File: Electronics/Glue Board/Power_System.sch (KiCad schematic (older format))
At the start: 10 parts, among them J1 Conn_01x02_Male, J2 Barrel_Jack, U6 TPS2121RUXR

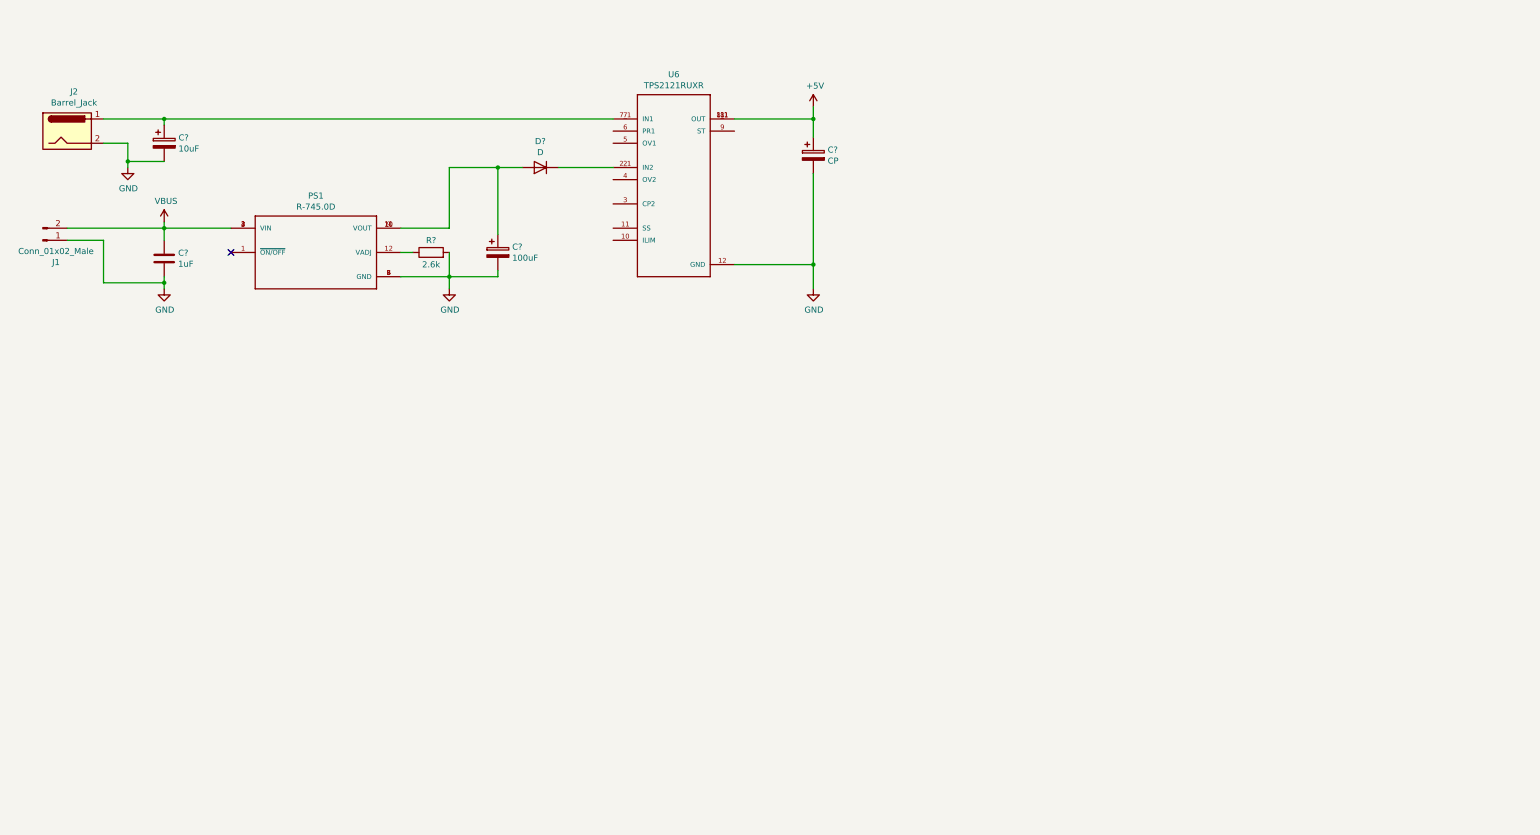
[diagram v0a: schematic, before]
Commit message: Finished the schematic for the most parts
Finished the schematic for the most parts
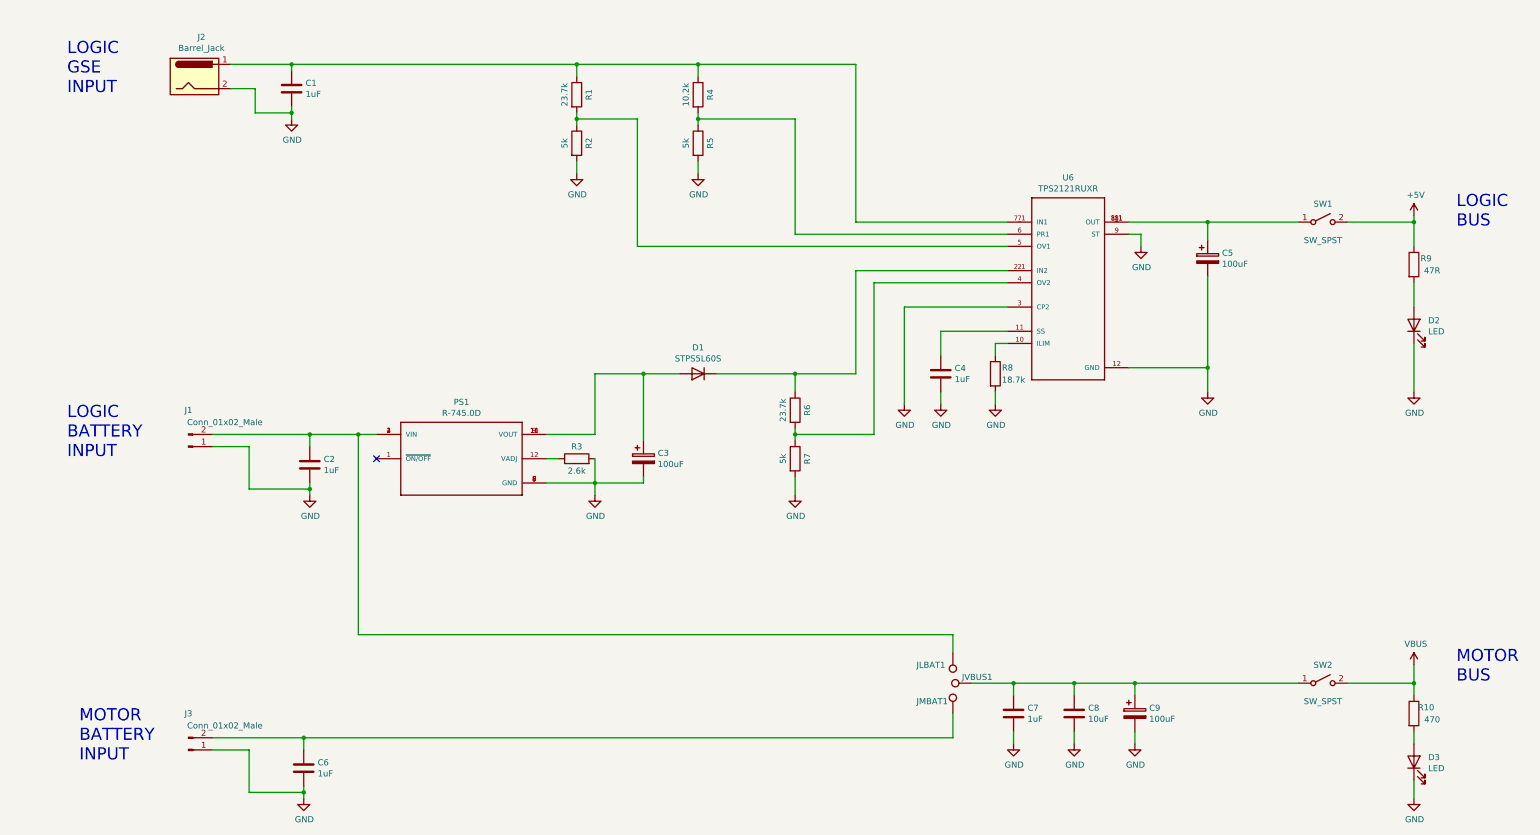
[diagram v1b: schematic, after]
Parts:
- removed C?: 10uF, symbol Device:CP
- added C1, C4, C6, C7: 1uF, Capacitor_SMD:C_0805_2012Metric, symbol Device:C
- added C8: 10uF, Capacitor_SMD:C_0805_2012Metric, symbol Device:C
- added C9: 100uF, Capacitor_SMD:C_1210_3225Metric, symbol Device:CP
- added D2, D3: LED, Connector_PinHeader_2.54mm:PinHeader_1x02_P2.54mm_Vertical, symbol Device:LED
- added J3: Conn_01x02_Male, Connector_AMASS:AMASS_XT30PW-M_1x02_P2.50mm_Horizontal, symbol Connector:Conn_01x02_Male
- added JLBAT1, JMBAT1, JVBUS1: TestPoint, TestPoint:TestPoint_Pad_D4.0mm, symbol Connector:TestPoint
- added R1, R6: 23.7k, Resistor_SMD:R_0603_1608Metric, symbol Device:R
- added R10: 470, Resistor_SMD:R_0603_1608Metric, symbol Device:R
- added R2, R5, R7: 5k, Resistor_SMD:R_0603_1608Metric, symbol Device:R
- added R4: 10.2k, Resistor_SMD:R_0603_1608Metric, symbol Device:R
- added R8: 18.7k, Resistor_SMD:R_0603_1608Metric, symbol Device:R
- added R9: 47R, Resistor_SMD:R_0603_1608Metric, symbol Device:R
- added SW1, SW2: SW_SPST, TerminalBlock:TerminalBlock_bornier-2_P5.08mm, symbol Switch:SW_SPST
- C2: renamed from C?; footprint (none) -> Capacitor_SMD:C_0805_2012Metric; MPN (none) -> C0805C105K4RACTU
- C3: renamed from C?; footprint (none) -> Capacitor_SMD:C_1210_3225Metric; MPN (none) -> C1210C107M4PAC7800
- C5: renamed from C?; value CP -> 100uF; footprint (none) -> Capacitor_SMD:C_1210_3225Metric; MPN (none) -> C1210C107M4PAC7800
- D1: renamed from D?; value D -> STPS5L60S; footprint (none) -> agg:DO-214AB-SMC; MPN (none) -> STPS5L60S
- PS1: Field4 9.10mm -> (none); Field5 RECOM -> (none); Field6 5 -> (none); MPN (none) -> R-745.0D
- R3: renamed from R?; footprint (none) -> Resistor_SMD:R_0603_1608Metric; MPN (none) -> RC0603FR-072K61L
- U6: Field4 Manufacturer Recommendations -> (none); MPN (none) -> TPS2121RUXR
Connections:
- net +5V: now also R9.1, SW1.2 (B); no longer C5.1, U6.1 (OUT), U6.1_1 (OUT), U6.8 (OUT), U6.8_1 (OUT)
- net GND: now also U6.3 (CP2), U6.9 (ST), C1.2, C4.2, C6.2, C7.2, C8.2, C9.2, D2.1 (K), D3.1 (K), J3.1 (Pin_1), R2.2, R5.2, R7.2, R8.2
- net VBUS: now also R10.1, SW2.2 (B); no longer C2.1, J1.2 (Pin_2), PS1.2 (VIN), PS1.3 (VIN), PS1.4 (VIN)
- net at U6.10 (ILIM): now also R8.1
- net at U6.11 (SS): now also C4.1
- net at D1.1 (K), U6.2 (IN2), U6.2_1 (IN2): now also R6.1
- net at U6.4 (OV2): now also R6.2, R7.1
- net at U6.5 (OV1): now also R1.2, R2.1
- net at U6.6 (PR1): now also R4.2, R5.1
- net at J2.1, U6.7 (IN1), U6.7_1 (IN1): now also C1.1, R1.1, R4.1
- new net: C2.1, J1.2 (Pin_2), JLBAT1.1, PS1.2 (VIN), PS1.3 (VIN), PS1.4 (VIN)
- new net: C5.1, SW1.1 (A), U6.1 (OUT), U6.1_1 (OUT), U6.8 (OUT), U6.8_1 (OUT)
- new net: C7.1, C8.1, C9.1, JVBUS1.1, SW2.1 (A)
- new net: C6.1, J3.2 (Pin_2), JMBAT1.1
- new net: D2.2 (A), R9.2
- new net: D3.2 (A), R10.2
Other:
- note added: "LOGIC\nBATTERY\nINPUT"
- note added: "LOGIC\nBUS"
- note added: "LOGIC\nGSE\nINPUT"
- note added: "MOTOR\nBATTERY\nINPUT"
- note added: "MOTOR\nBUS"
- moved on the sheet: C2, C3, C5, D1, J1, J2, PS1, R3, U6

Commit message: Complete Schematic and BOM
Complete Schematic and BOM. Next up, layout!
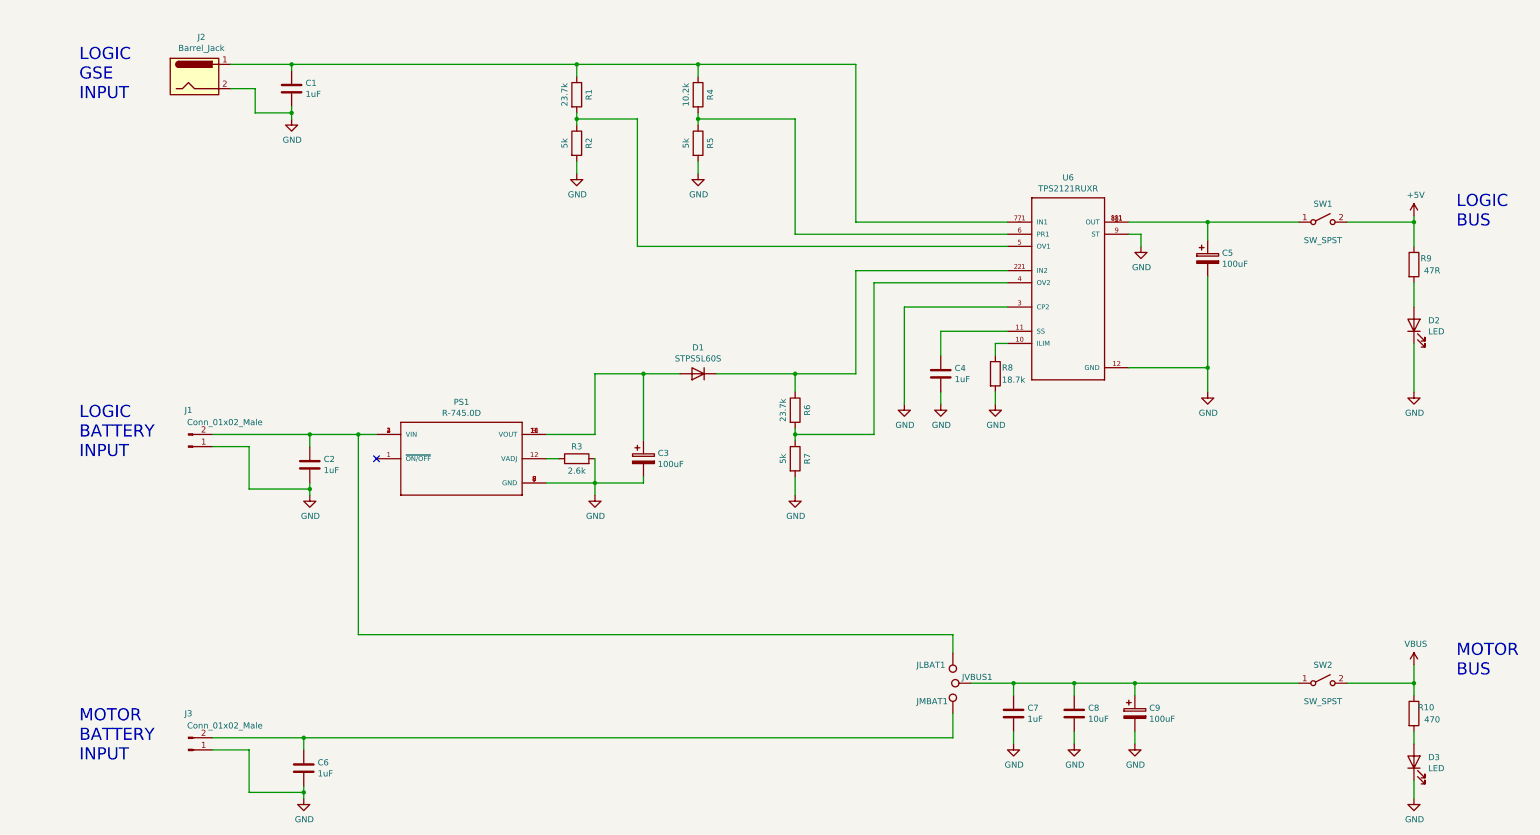
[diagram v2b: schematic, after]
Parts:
- J1, J3: MPN (none) -> XT30PW-M
- J2: MPN (none) -> PJ-102B
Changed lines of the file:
@@
 encoding utf-8
 Sheet 2 5
-Title ""
-Date ""
-Rev ""
+Title "Robocar, Pinky, Power System"
+Date "2019-12-28"
+Rev "A"
 Comp ""
 Comment1 ""
@@
 F 2 "Connector_BarrelJack:BarrelJack_Horizontal" H 3450 2010 50  0001 C CNN
 F 3 "~" H 3450 2010 50  0001 C CNN
+F 4 "PJ-102B" H 3400 2050 50  0001 C CNN "MPN"
 	1    3400 2050
 	1    0    0    -1
@@
 F 2 "Connector_AMASS:AMASS_XT30PW-M_1x02_P2.50mm_Horizontal" H 3350 5100 50  0001 C CNN
 F 3 "~" H 3350 5100 50  0001 C CNN
+F 4 "XT30PW-M" H 3350 5100 50  0001 C CNN "MPN"
 	1    3350 5100
 	1    0    0    1
@@
 Wire Wire Line
 	11200 3350 11200 3450
-Text Notes 2350 2200 0    100  ~ 0
+Text Notes 2450 2250 0    100  ~ 0
 LOGIC\nGSE\nINPUT
-Text Notes 2350 5200 0    100  ~ 0
+Text Notes 2450 5200 0    100  ~ 0
 LOGIC\nBATTERY\nINPUT
-Text Notes 13800 7050 0    100  ~ 0
+Text Notes 13800 7000 0    100  ~ 0
 MOTOR\nBUS
 Text Notes 13800 3300 0    100  ~ 0
@@
 F 2 "Connector_AMASS:AMASS_XT30PW-M_1x02_P2.50mm_Horizontal" H 3350 7600 50  0001 C CNN
 F 3 "~" H 3350 7600 50  0001 C CNN
+F 4 "XT30PW-M" H 3350 7600 50  0001 C CNN "MPN"
 	1    3350 7600
 	1    0    0    1

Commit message: Added Motor v-sense and battery mon. Layout time!
Added Motor v-sense and battery mon. Layout time!
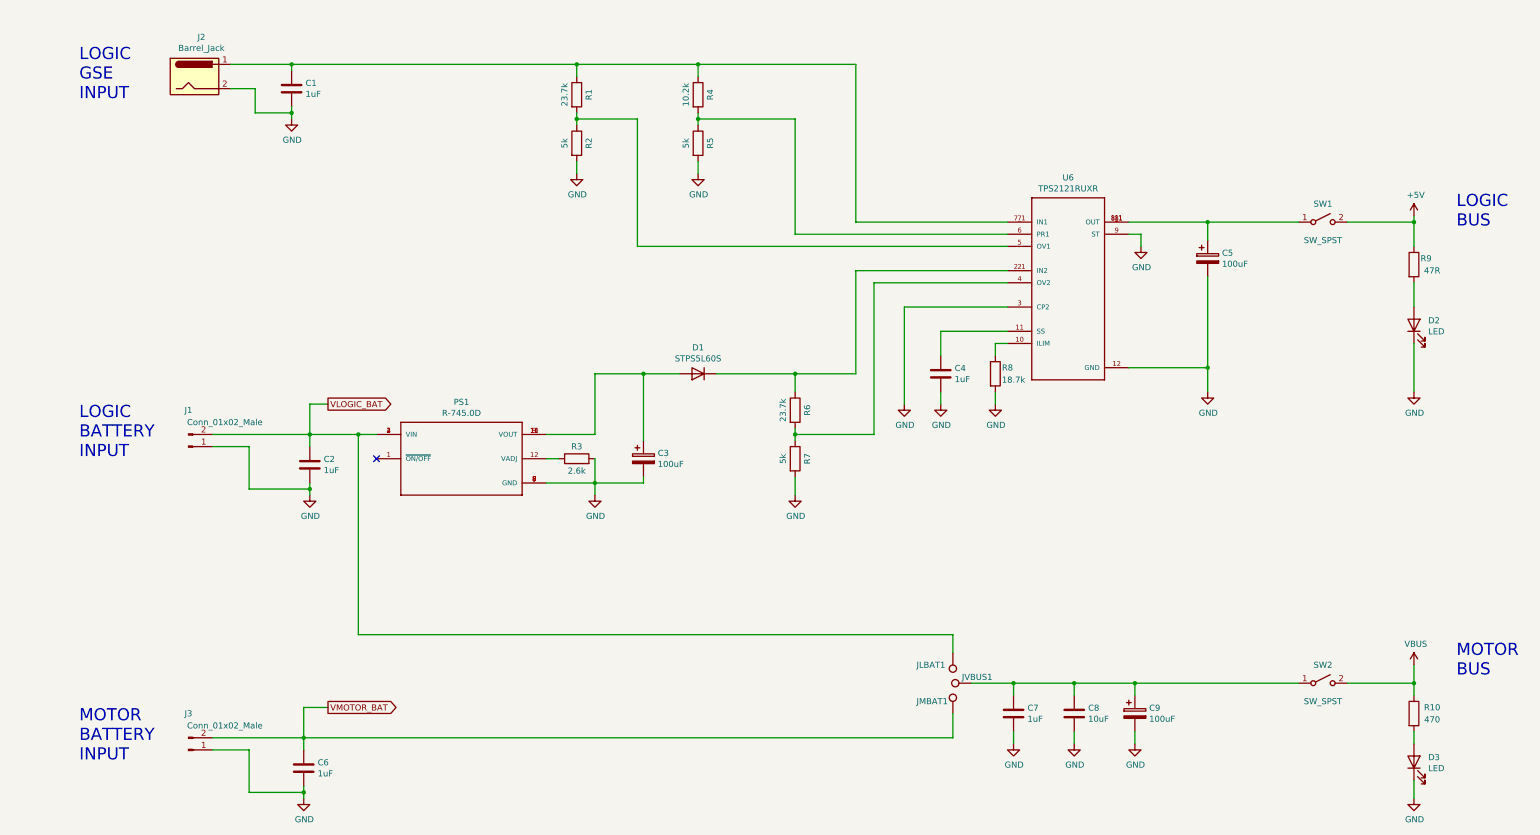
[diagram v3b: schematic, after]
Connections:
- net VLOGIC_BAT: now reaches C2.1, J1.2 (Pin_2), JLBAT1.1, PS1.2 (VIN), PS1.3 (VIN), PS1.4 (VIN)
- net VMOTOR_BAT: now reaches C6.1, J3.2 (Pin_2), JMBAT1.1
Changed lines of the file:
@@
 U 1 1 5E188924
 P 13450 7300
-F 0 "R10" H 13550 7350 50  0000 C CNN
+F 0 "R10" H 13600 7350 50  0000 C CNN
 F 1 "470" H 13600 7250 50  0000 C CNN
 F 2 "Resistor_SMD:R_0603_1608Metric" V 13380 7300 50  0001 C CNN
@@
 Wire Wire Line
 	13450 7850 13450 8000
+Text GLabel 4500 7250 2    50   Output ~ 0
+VMOTOR_BAT
+Text GLabel 4500 4750 2    50   Output ~ 0
+VLOGIC_BAT
+Wire Wire Line
+	4500 4750 4350 4750
+Wire Wire Line
+	4350 4750 4350 5000
+Wire Wire Line
+	4500 7250 4300 7250
+Wire Wire Line
+	4300 7250 4300 7500
 $EndSCHEMATC

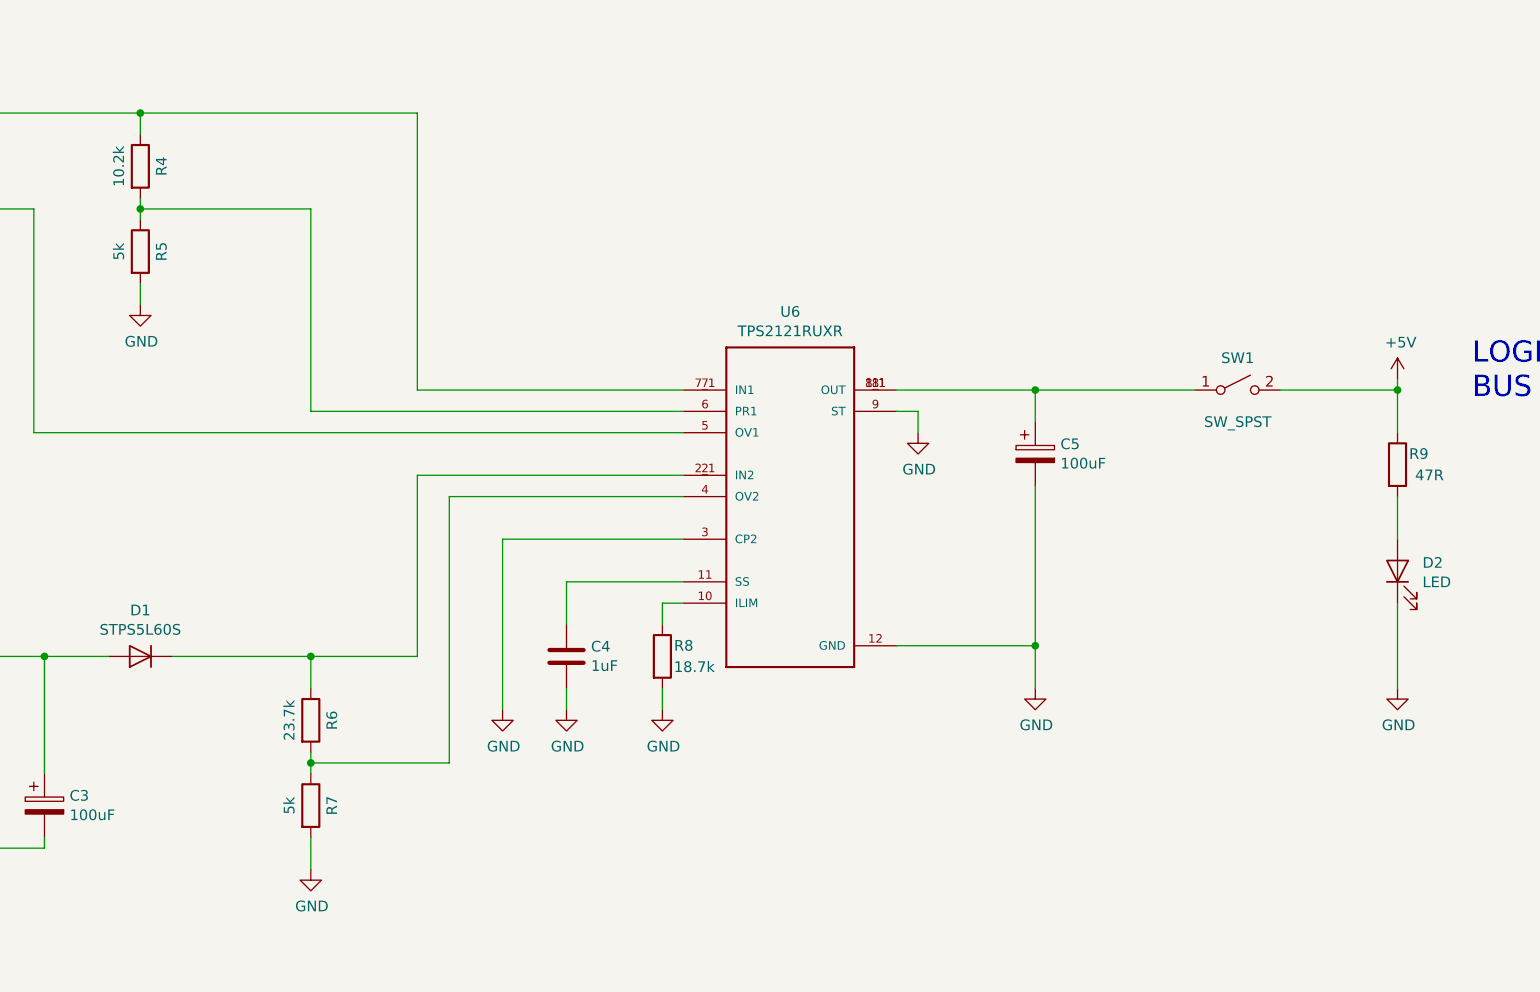
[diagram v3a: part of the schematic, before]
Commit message: Abandoned oCamS for ZED Mini and updated Glue Board
Abandoned oCamS for ZED Mini and updated Glue Board
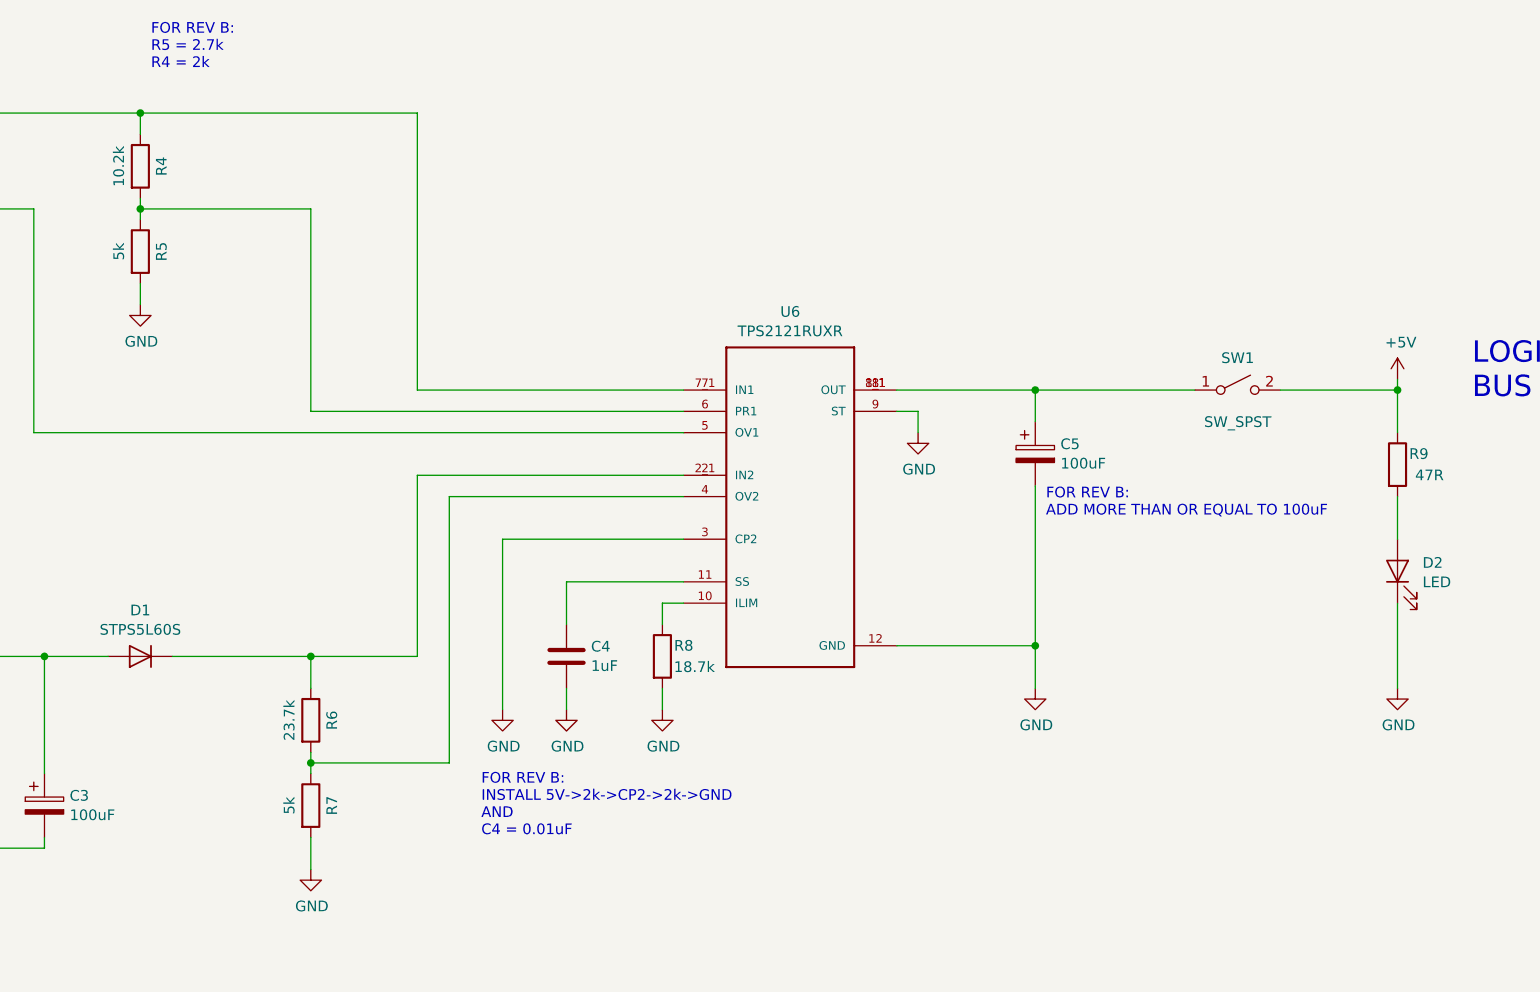
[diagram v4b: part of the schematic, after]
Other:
- note added: "FOR REV B:\nADD MORE THAN OR EQUAL TO 100uF"
- note added: "FOR REV B:\nINSTALL 5V->2k->CP2->2k->GND\nAND\nC4 = 0.01uF\n"
- note added: "FOR REV B:\nR5 = 2.7k\nR4 = 2k"
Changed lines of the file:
@@
 Wire Wire Line
 	4300 7250 4300 7500
+Text Notes 9150 5350 0    50   ~ 0
+FOR REV B:\nINSTALL 5V->2k->CP2->2k->GND\nAND\nC4 = 0.01uF\n
+Text Notes 7600 1750 0    50   ~ 0
+FOR REV B:\nR5 = 2.7k\nR4 = 2k
+Text Notes 11800 3850 0    50   ~ 0
+FOR REV B:\nADD MORE THAN OR EQUAL TO 100uF
 $EndSCHEMATC
